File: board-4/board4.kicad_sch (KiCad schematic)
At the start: 101 parts

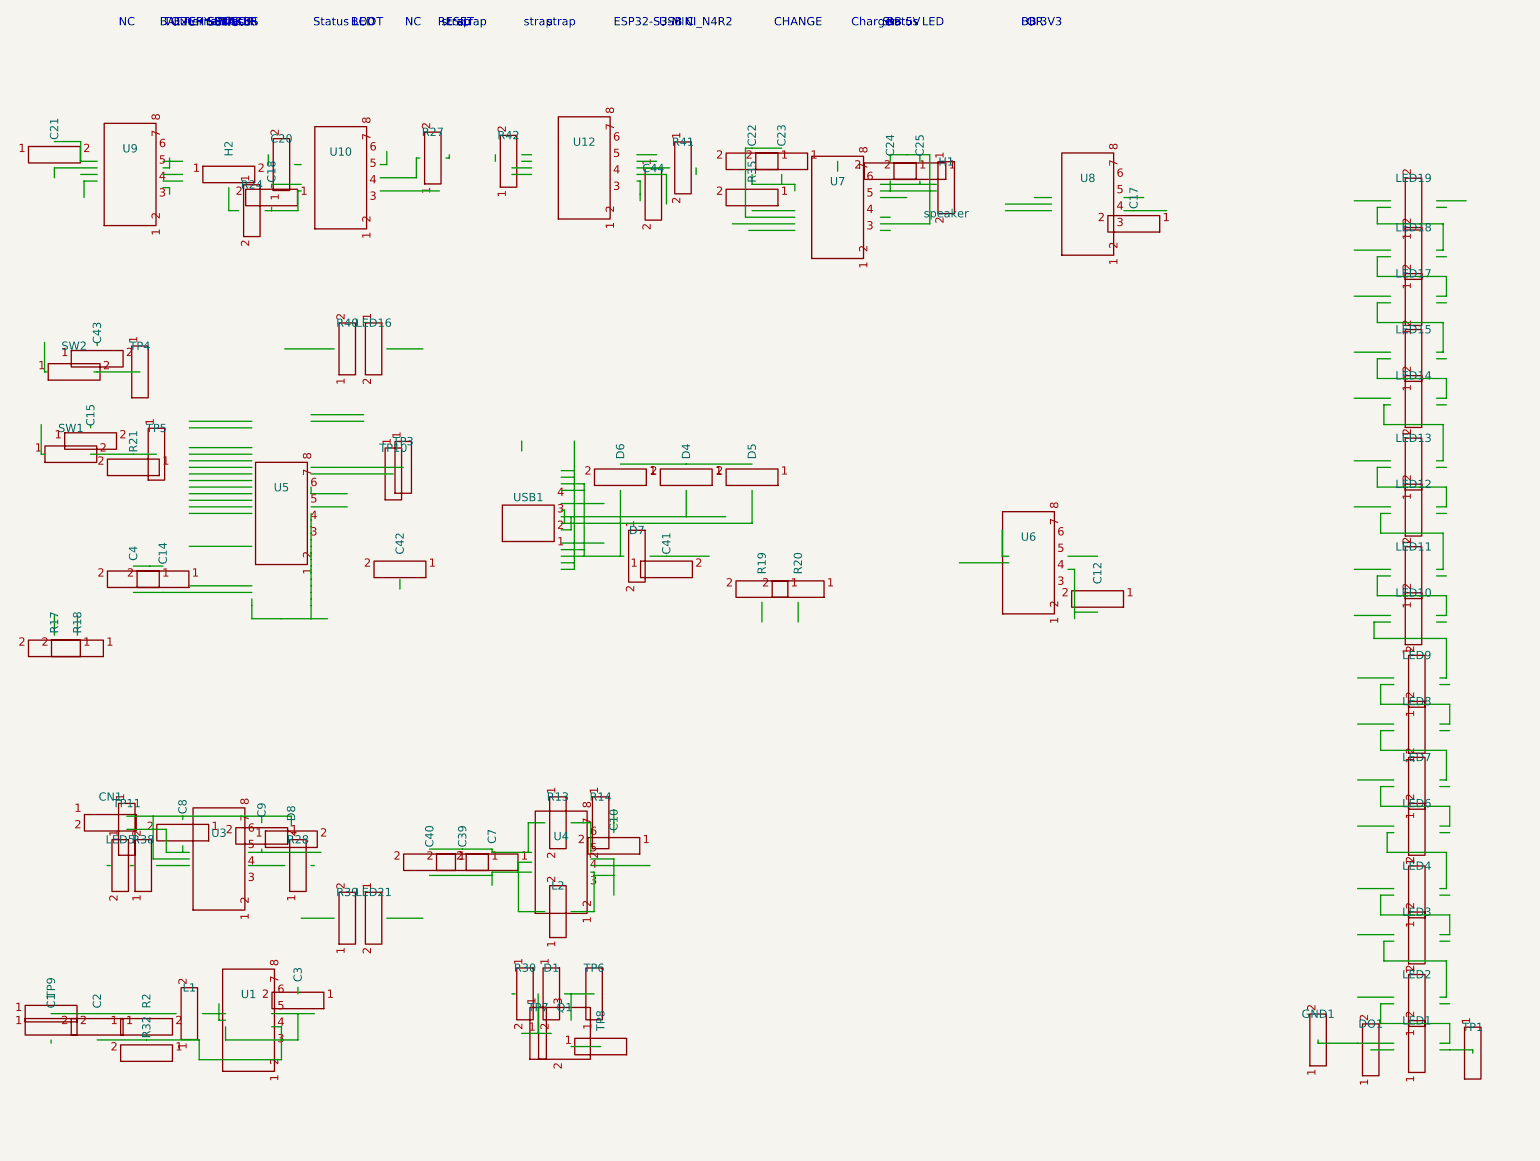
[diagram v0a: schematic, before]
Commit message: Schematic: use real .esym geometry — 39 of 44 lib_symbols built from EasyEDA source (proper pins, no more red placeholders)
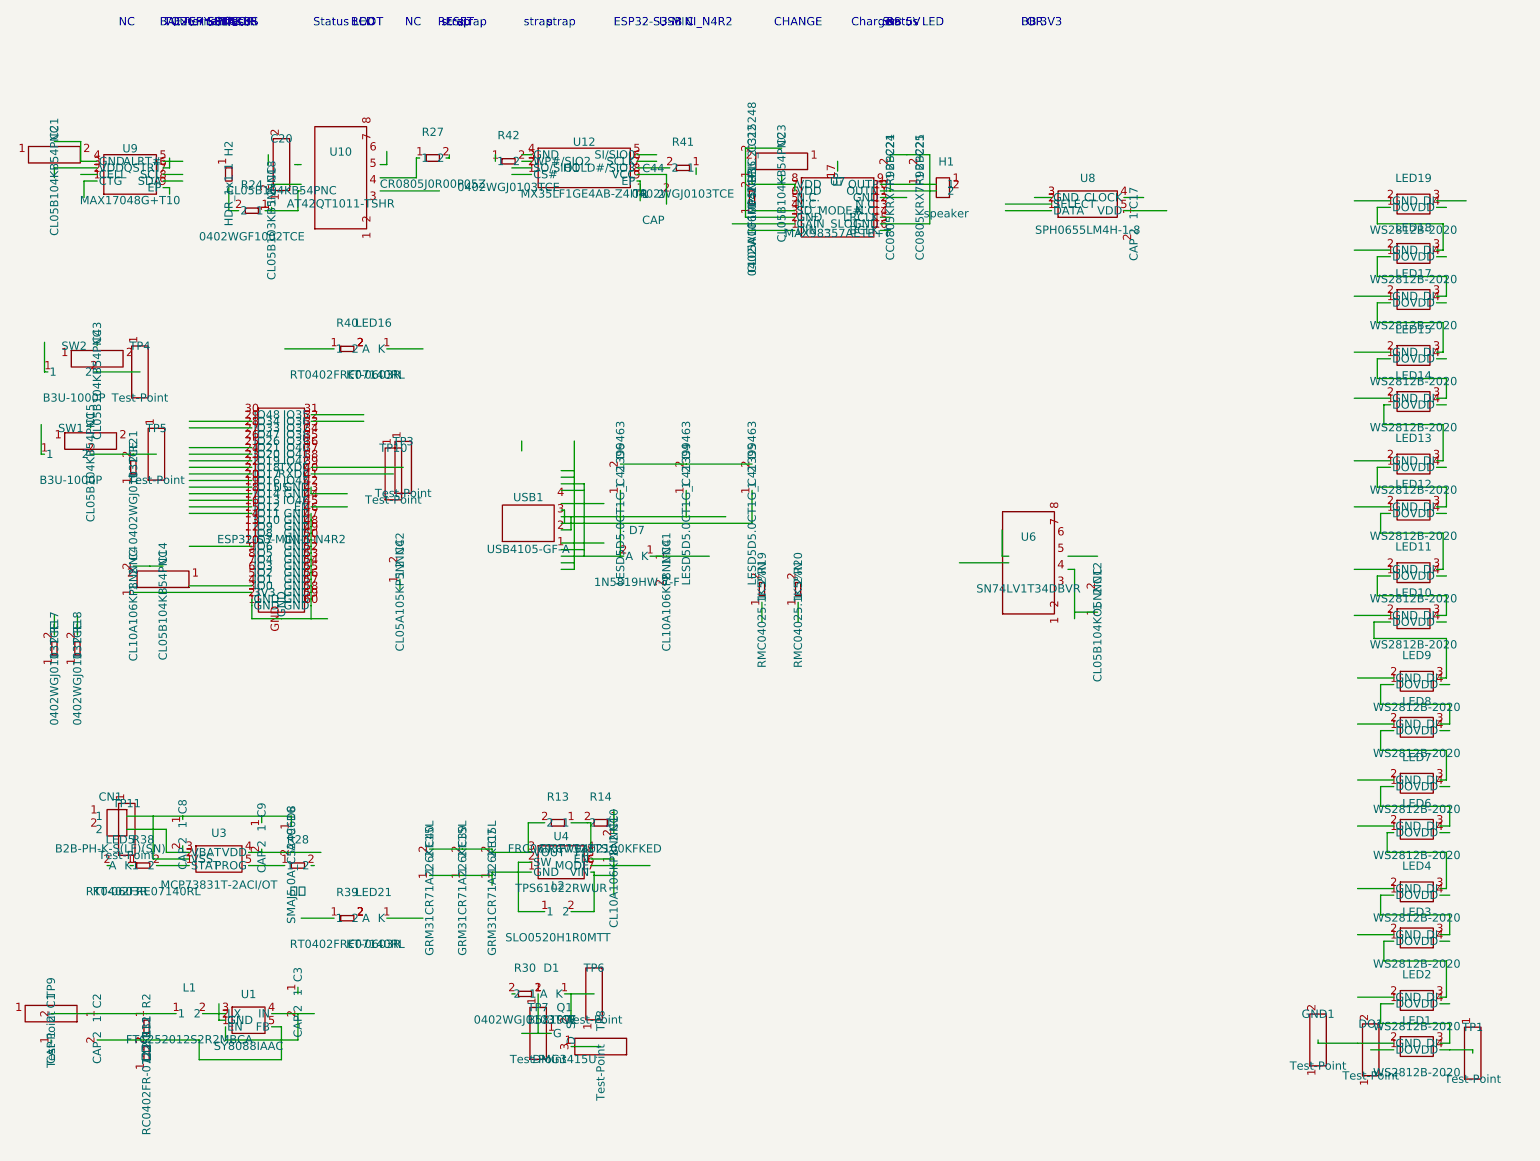
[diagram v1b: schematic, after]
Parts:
- removed C1, C10, C12, C17, C18, C2, C22, C24, C25, C3, C39, C4, C40, C41, C42, C44, C7, C8, C9: (no value), symbol Device:C
- removed CN1: (no value), symbol Connector:Conn_01x02
- removed D1, D4, D5, D6, D7, D8: (no value), symbol Device:D
- removed H1: speaker, symbol Device:R
- removed H2, R13, R14, R17, R18, R19, R2, R20, R21, R24, R27, R28, R30, R32, R35, R38, R39, R40, R41, R42: (no value), symbol Device:R
- removed L1, L2: (no value), symbol Device:L
- removed LED1, LED10, LED11, LED12, LED13, LED14, LED15, LED16, LED17, LED18, LED19, LED2, LED21, LED3, LED4, LED5, LED6, LED7, LED8, LED9: (no value), symbol Device:LED
- removed Q1: (no value), symbol Device:Q_NPN_BCE
- removed SW1, SW2: (no value), symbol Switch:SW_Push
- removed U1, U12, U3, U4, U5, U7, U8, U9: (no value), symbol Connector_Generic:Conn_01x08
- added C1, C17, C2, C3, C44, C8, C9: CAP, symbol EasyEDA:CAP_7b3e0fe7
- added C10, C4, C41: CL10A106KP8NNNC, symbol EasyEDA:CL10A106KP8NNNC_95a8ba2b
- added C12: CL05B104KO5NNNC, symbol EasyEDA:CL05B104KO5NNNC_97b14fdc
- added C18: CL05B103KB5NNNC, symbol EasyEDA:CL05B103KB5NNNC_24fe9c11
- added C22: CL05A106MP5NUNC_C315248, symbol EasyEDA:CL05A106MP5NUNC_C315248_132c4d86
- added C24, C25: CC0805KRX7R9BB221, symbol EasyEDA:CC0805KRX7R9BB221_b1bb5d50
- added C39, C40, C7: GRM31CR71A226KE15L, symbol EasyEDA:GRM31CR71A226KE15L_288ce33a
- added C42: CL05A105KP5NNNC, symbol EasyEDA:CL05A105KP5NNNC_c070375c
- added CN1: B2B-PH-K-S(LF)(SN), symbol EasyEDA:B2B-PH-K-S_LF__SN__e8672a3e
- added D1: B5819W, symbol EasyEDA:B5819W_9595a8c7
- added D4, D5, D6: LESD5D5.0CT1G_C41399463, symbol EasyEDA:LESD5D5_0CT1G_C41399463_a64f8fb1
- added D7: 1N5819HW-7-F, symbol EasyEDA:1N5819HW-7-F_95873cba
- added D8: SMAJ5.0A_C5249616, symbol EasyEDA:SMAJ5_0A_C5249616_d20bd494
- added H1: speaker, symbol EasyEDA:Header-Female-2_54_1x2_31abfba7
- added H2: HDR_1x1, symbol EasyEDA:HDR_1x1_bd9b80ac
- added L1: FTC252012S2R2MBCA, symbol EasyEDA:FTC252012S2R2MBCA_24f015e0
- added L2: SLO0520H1R0MTT, symbol EasyEDA:SLO0520H1R0MTT_18485827
- added LED1, LED10, LED11, LED12, LED13, LED14, LED15, LED17, LED18, LED19, LED2, LED3, LED4, LED6, LED7, LED8, LED9: WS2812B-2020, symbol EasyEDA:WS2812B-2020_8fe14a7c
- added LED16, LED21, LED5: KT-0603R, symbol EasyEDA:KT-0603R_f45a963b
- added Q1: DMG3415U, symbol EasyEDA:DMG3415U_309928de
- added R13: FRC0603F7323TS, symbol EasyEDA:FRC0603F7323TS_17e71eb3
- added R14: CRCW0402100KFKED, symbol EasyEDA:CRCW0402100KFKED_b191eefb
- added R17, R18, R21, R30, R41, R42: 0402WGJ0103TCE, symbol EasyEDA:0402WGJ0103TCE_acbc32fa
- added R19, R20: RMC04025.1K5%N, symbol EasyEDA:RMC04025_1K5_N_27becd8d
- added R2, R28: 电阻, symbol EasyEDA:___7f0b4804
- added R24: 0402WGF1002TCE, symbol EasyEDA:0402WGF1002TCE_a6ad73aa
- added R27: CR0805J0R00P05Z, symbol EasyEDA:CR0805J0R00P05Z_d8752634
- added R32: RC0402FR-0722K1L, symbol EasyEDA:RC0402FR-0722K1L_014052d2
- added R35: 0402WGF1004TCE, symbol EasyEDA:0402WGF1004TCE_816cca08
- added R38, R39, R40: RT0402FRE07140RL, symbol EasyEDA:RT0402FRE07140RL_39db32a2
- added SW1, SW2: B3U-1000P, symbol EasyEDA:B3U-1000P_7a76bde0
- added U1: SY8088IAAC, symbol EasyEDA:SY8088IAAC_85109f5b
- added U12: MX35LF1GE4AB-Z4ITR, symbol EasyEDA:MX35LF1GE4AB-Z4ITR_3b0d5531
- added U3: MCP73831T-2ACI/OT, symbol EasyEDA:MCP73831T-2ACI_OT_f97c5b68
- added U4: TPS61022RWUR, symbol EasyEDA:TPS61022RWUR_bdebc0ab
- added U5: ESP32-S3-MINI-1-N4R2, symbol EasyEDA:ESP32-S3-MINI-1-N4R2_d7e8eeba
- added U7: MAX98357AETE+T, symbol EasyEDA:MAX98357AETE_T_347486d5
- added U8: SPH0655LM4H-1-8, symbol EasyEDA:SPH0655LM4H-1-8_3964195d
- added U9: MAX17048G+T10, symbol EasyEDA:MAX17048G_T10_6b2d9a5b
- C14, C15, C20, C21, C23, C43: value (none) -> CL05B104KB54PNC
- DO1, GND1, TP1, TP10, TP11, TP3, TP4, TP5, TP6, TP7, TP8, TP9: value (none) -> Test-Point
- U10: value (none) -> AT42QT1011-TSHR
- U6: value (none) -> SN74LV1T34DBVR
- USB1: value (none) -> USB4105-GF-A
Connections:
- new net: LED1.3 (DI), LED2.1 (DO)
- new net: LED2.3 (DI), LED3.1 (DO)
- new net: C1.2, C2.1, L1.1, R2.1
- new net: LED21.2 (A), R39.2
- new net: D4.2, D5.2, D6.2
- new net: C39.1, C40.1, C7.1, U4.1 (GND)
- new net: C39.2, C40.2, C7.2, R13.2, U4.3 (VOUT)
- new net: R28.1, U3.5 (PROG)
- new net: LED8.3 (DI), LED9.1 (DO)
- new net: LED10.1 (DO), LED9.3 (DI)
- new net: R42.2, U12.3 (WP#/SIO2)
- new net: C3.2, U1.1 (EN), U1.4 (IN)
- new net: LED18.3 (DI), LED19.1 (DO)
- new net: LED16.2 (A), R40.2
- new net: R21.2, SW1.2
- new net: C10.1, L2.2, U4.5 (EN), U4.7 (VIN)
- new net: C10.2, R14.1
- new net: LED6.3 (DI), LED7.1 (DO)
- new net: LED7.3 (DI), LED8.1 (DO)
- new net: C22.1, R35.2, U7.7 (VDD), U7.8 (VDD)
- new net: C22.2, U7.3 (GND)
- new net: C18.1, R24.1
- new net: C2.2, R2.2, R32.2, U1.5 (FB)
- new net: C41.1, D7.1 (K)
- new net: D6.1, D7.2 (A)
- new net: LED10.3 (DI), LED11.1 (DO)
- new net: LED11.3 (DI), LED12.1 (DO)
- new net: L2.1, U4.2 (SW)
- new net: C24.1, U7.10 (OUTN)
- new net: C24.2, C25.2, U7.15 (GND)
- new net: LED13.3 (DI), LED14.1 (DO)
- new net: LED14.3 (DI), LED15.1 (DO)
- new net: D1.2 (A), Q1.1 (G), R30.1
- new net: C8.1, C9.1, D8.1 (C), U3.2 (VSS)
- new net: C9.2, D8.2 (A), U3.4 (VDD)
- new net: LED15.3 (DI), LED17.1 (DO)
- new net: R13.1, R14.2, U4.4 (FB)
- new net: LED4.3 (DI), LED6.1 (DO)
- new net: C4.1, U5.3 (3V3)
- new net: U5.1 (GND), U5.2 (GND), U5.46 (GND), U5.47 (GND), U5.48 (GND), U5.49 (GND), U5.50 (GND), U5.51 (GND), U5.52 (GND), U5.53 (GND), U5.54 (GND), U5.55 (GND), U5.56 (GND), U5.57 (GND), U5.58 (GND), U5.59 (GND), U5.60 (GND), U5.GND
- new net: U5.42 (GND), U5.43 (GND)
- new net: C44.1, U12.9 (EP)
- new net: C44.2, U12.8 (VCC)
- new net: D1.1 (K), Q1.2 (S)
- new net: LED17.3 (DI), LED18.1 (DO)
- new net: R35.1, U7.4 (SD_MODE#)
- new net: C25.1, U7.9 (OUTP)
- new net: LED12.3 (DI), LED13.1 (DO)
- new net: R41.2, U12.7 (HOLD#/SIO3)
- new net: LED3.3 (DI), LED4.1 (DO)
- new net: L1.2, U1.3 (LX)
- new net: LED5.1 (K), R38.1
- new net: C8.2, U3.3 (VBAT)
- new net: C17.1, U8.5 (VDD)
- new net: R38.2, U3.1 (STAT)

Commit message: Add LCSC component library: 48 components now render with real 3D bodies. Schematic adds 154 NET labels + 17 global labels + 27 no_connects from .esch (was missing).
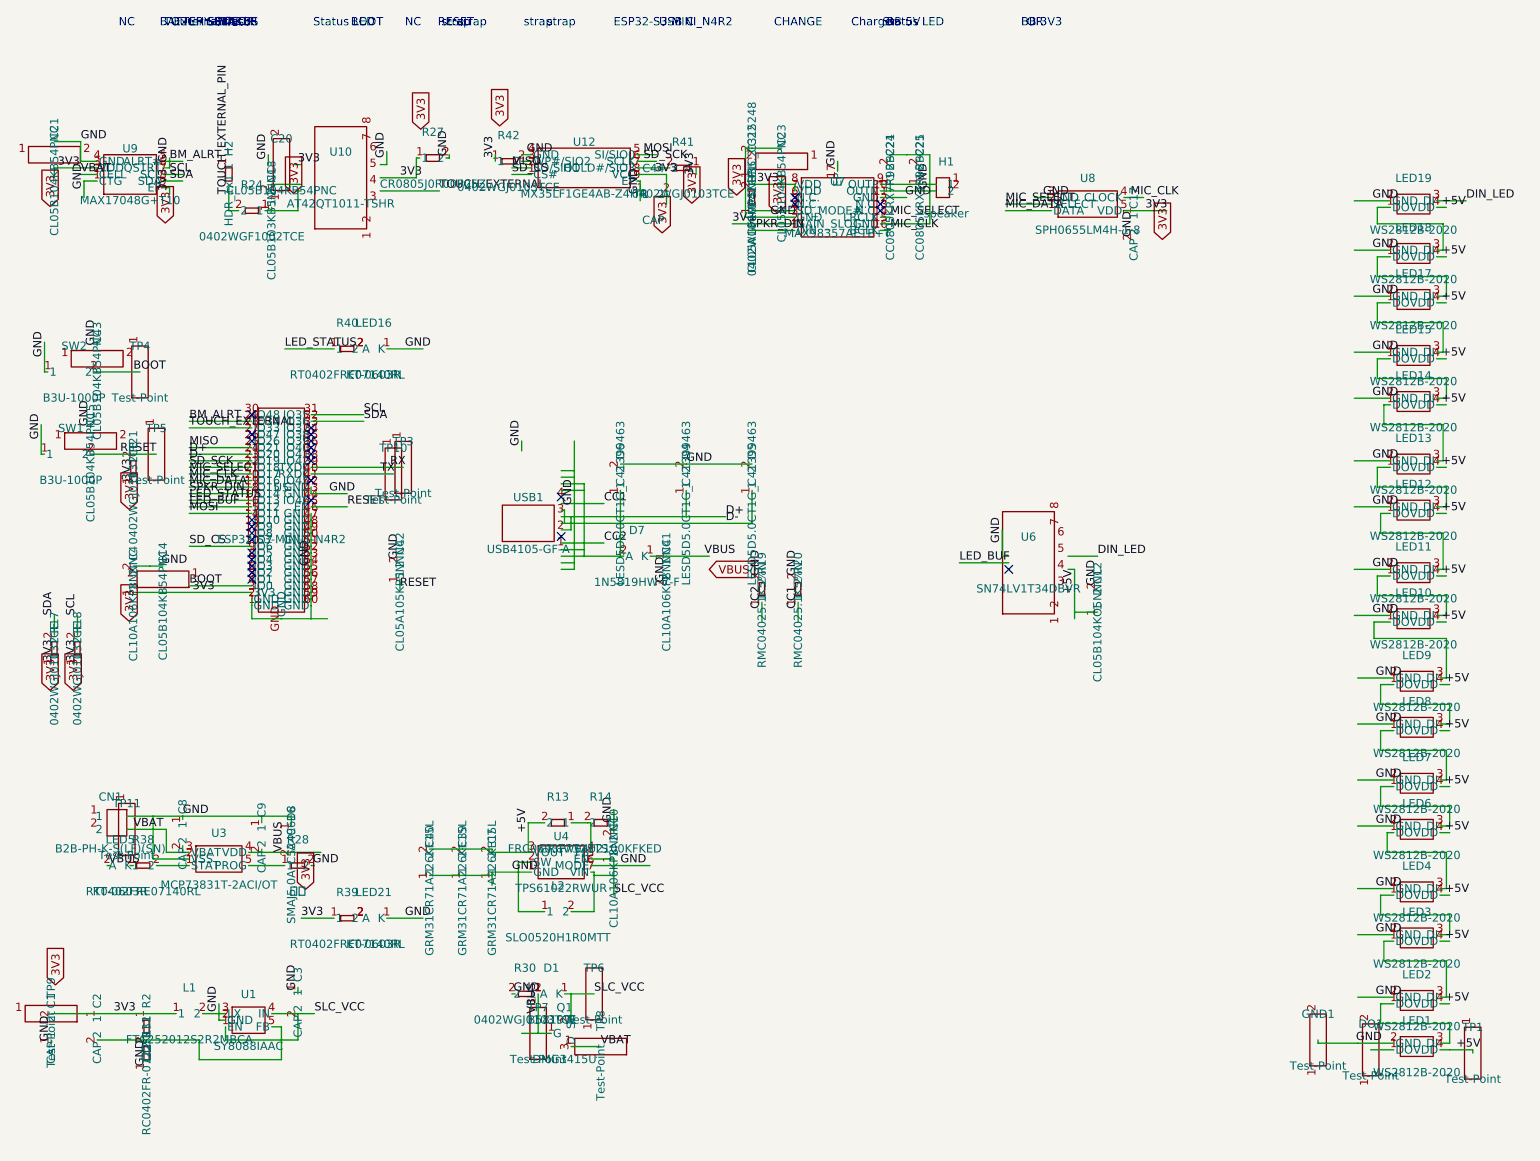
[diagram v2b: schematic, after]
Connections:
- net BM_ALRT: now reaches U9.1 (CTG)
- net BM_ALRT: now also C1.1, C10.2, C12.2, C17.2, C22.2, C24.2, C25.2, C3.1, C39.1, C4.2, C40.1, C41.2, C42.2, C44.1, C7.1, C8.1, C9.1, D4.2, D5.2, D6.2, D8.1 (C), LED1.2 (GND), LED10.2 (GND), LED11.2 (GND), LED12.2 (GND), LED13.2 (GND), LED14.2 (GND), LED15.2 (GND), LED16.1 (K), LED17.2 (GND), LED18.2 (GND), LED19.2 (GND), LED2.2 (GND), LED21.1 (K), LED3.2 (GND), LED4.2 (GND), LED6.2 (GND), LED7.2 (GND), LED8.2 (GND), LED9.2 (GND), R14.1, R19.2, R20.2, R27.2, R28.2, R30.2, R32.1, SW1.1, SW2.1, U1.2 (GND), U12.4 (GND), U12.9 (EP), U3.2 (VSS), U4.1 (GND), U4.6 (MODE), U5.1 (GND), U5.2 (GND), U5.29 (IO34), U5.42 (GND), U5.43 (GND), U5.46 (GND), U5.47 (GND), U5.48 (GND), U5.49 (GND), U5.50 (GND), U5.51 (GND), U5.52 (GND), U5.53 (GND), U5.54 (GND), U5.55 (GND), U5.56 (GND), U5.57 (GND), U5.58 (GND), U5.59 (GND), U5.60 (GND), U5.GND, U7.11 (GND), U7.15 (GND), U7.17 (EP), U7.3 (GND), U8.3 (GND), U9.4 (GND), U9.5 (ALRT#), U9.6 (QSTRT)
- net VBAT: now reaches U9.2 (CELL)
- net VBAT: now also C8.2, Q1.3 (D), U3.3 (VBAT)
- net 3V3: now reaches U9.3 (VDD)
- net 3V3: now also C1.2, C17.1, C2.1, C22.1, C4.1, C44.2, L1.1, R17.1, R18.1, R2.1, R21.1, R27.1, R35.2, R39.1, R41.1, R42.1, U12.8 (VCC), U5.3 (3V3), U7.2 (GAIN_SLOT), U7.7 (VDD), U7.8 (VDD), U8.5 (VDD), U9.9 (EP)
- net SCL: now reaches U9.7 (SCL)
- net SCL: now also R18.2, U5.31 (IO35)
- net SDA: now reaches U9.8 (SDA)
- net SDA: now also R17.2, U5.32 (IO36)
- net +5V: now reaches LED2.4 (VDD)
- net +5V: now also C12.1, C39.2, C40.2, C7.2, LED1.4 (VDD), LED10.4 (VDD), LED11.4 (VDD), LED12.4 (VDD), LED13.4 (VDD), LED14.4 (VDD), LED15.4 (VDD), LED17.4 (VDD), LED18.4 (VDD), LED19.4 (VDD), LED3.4 (VDD), LED4.4 (VDD), LED6.4 (VDD), LED7.4 (VDD), LED8.4 (VDD), LED9.4 (VDD), R13.2, U4.3 (VOUT)
- net D-: now reaches D5.1
- net D-: now also U5.23 (IO19)
- net SLC_VCC: now reaches C3.2, U1.1 (EN), U1.4 (IN)
- net SLC_VCC: now also C10.1, D1.1 (K), L2.2, Q1.2 (S), U4.5 (EN), U4.7 (VIN)
- net DIN_LED: now reaches LED19.3 (DI)
- net LED_STATUS: now reaches R40.1
- net LED_STATUS: now also U5.17 (IO13)
- net RESET: now reaches R21.2, SW1.2
- net RESET: now also C42.1, U5.45 (EN)
- net VBUS: now reaches C41.1, D7.1 (K)
- net VBUS: now also C9.2, D1.2 (A), D8.2 (A), LED5.2 (A), Q1.1 (G), R30.1, U3.4 (VDD)
- net CC2: now reaches R19.1
- net CC1: now reaches R20.1
- net SD_CS: now reaches U5.10 (IO6)
- net SD_CS: now also U12.1 (CS#)
- net MOSI: now reaches U5.15 (IO11)
- net MOSI: now also U12.5 (SI/SIO0)
- net LED_BUF: now reaches U5.16 (IO12)
- net SPKR_DIN: now reaches U5.18 (IO14)
- net SPKR_DIN: now also U7.1 (DIN)
- net MIC_DATA: now reaches U5.19 (IO15)
- net MIC_DATA: now also U8.1 (DATA)
- net MIC_CLK: now reaches U5.20 (IO16)
- net MIC_CLK: now also U7.16 (BCLK), U8.4 (CLOCK)
- net MIC_SELECT: now reaches U5.21 (IO17)
- net MIC_SELECT: now also U7.14 (LRCLK), U8.2 (SELECT)
- net SD_SCK: now reaches U5.22 (IO18)
- net SD_SCK: now also U12.6 (SCLK)
- net D+: now reaches U5.24 (IO20)
- net D+: now also D4.1
- net MISO: now reaches U5.25 (IO21)
- net MISO: now also U12.2 (SO/SIO1)
- net TOUCH_EXTERNAL: now reaches U5.28 (IO33)
- net RX: now reaches U5.39 (TXD0)
- net BOOT: now reaches U5.4 (IO0)
- net BOOT: now also SW2.2
- net TX: now reaches U5.40 (RXD0)
- net TOUCH_EXTERNAL_PIN: now reaches R24.2
- no-connect marks 0 -> 27
